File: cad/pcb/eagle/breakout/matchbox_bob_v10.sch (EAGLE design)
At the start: 9 parts, among them J1 DF12-32-DS, J2 DF12-32-DS

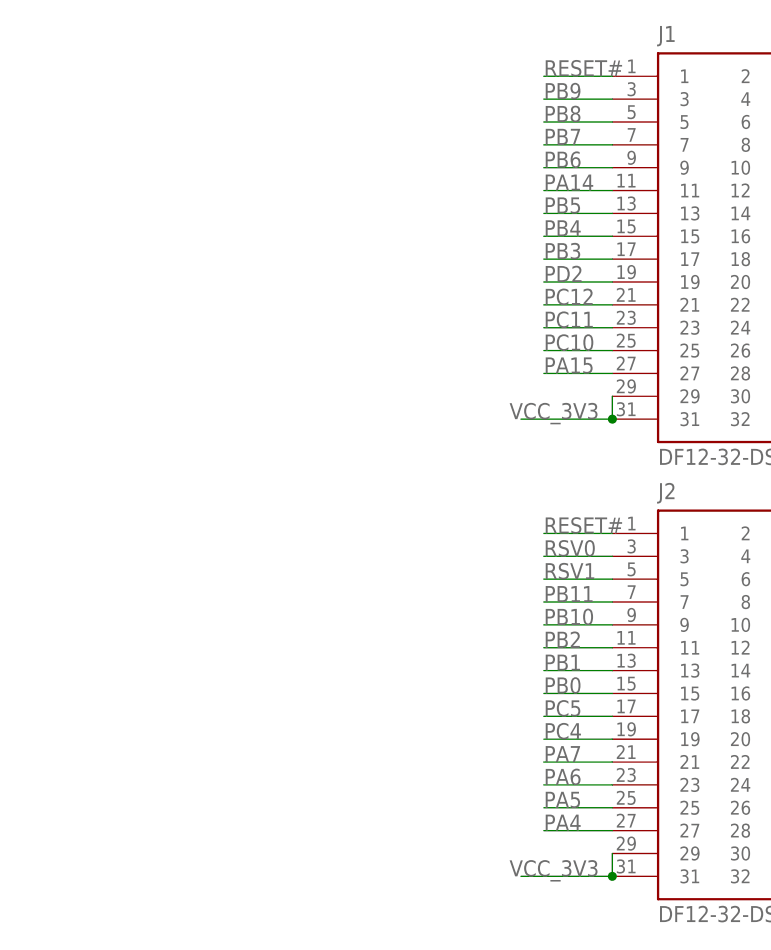
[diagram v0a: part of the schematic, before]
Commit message: Tweaks to BOB v1.0
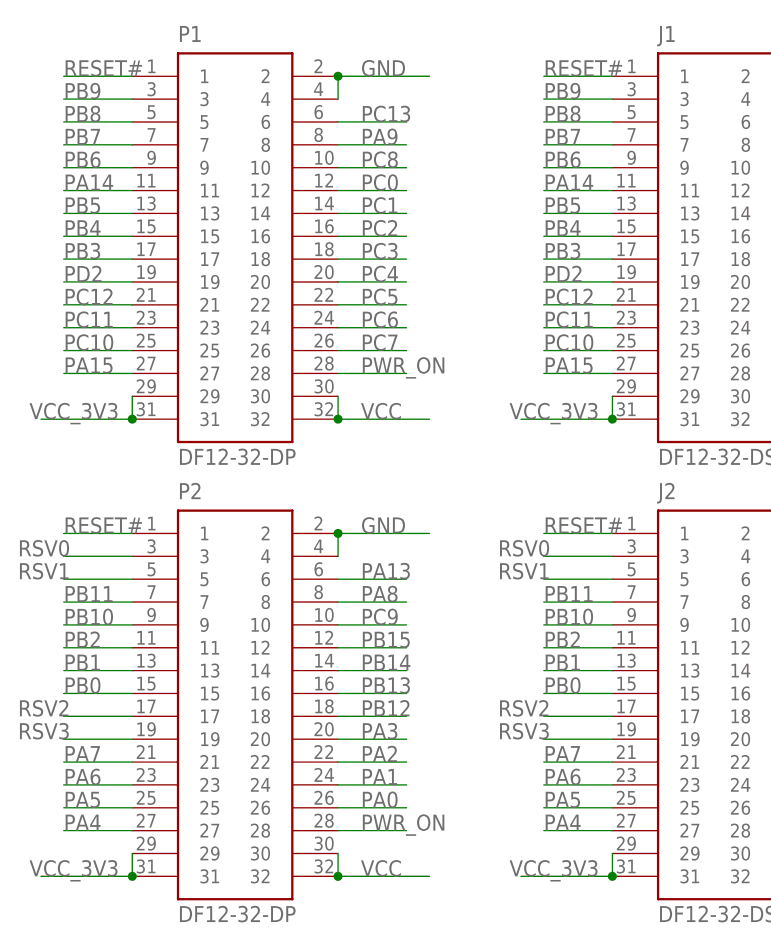
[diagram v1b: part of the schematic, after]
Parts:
- added P1, P2: DF12-32-DP, micro1292:AS-ITM-00015
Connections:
- new net RSV2: J2.17, P2.17
- new net RSV3: J2.19, P2.19
- net GND: now also P1.2, P1.4, P2.2, P2.4
- net PA0: now also P2.26
- net PA1: now also P2.24
- net PA13: now also P2.6
- net PA14: now also P1.11
- net PA15: now also P1.27
- net PA2: now also P2.22
- net PA3: now also P2.20
- net PA4: now also P2.27
- net PA5: now also P2.25
- net PA6: now also P2.23
- net PA7: now also P2.21
- net PA8: now also P2.8
- net PA9: now also P1.8
- net PB0: now also P2.15
- net PB1: now also P2.13
- net PB10: now also P2.9
- net PB11: now also P2.7
- net PB12: now also P2.18
- net PB13: now also P2.16
- net PB14: now also P2.14
- net PB15: now also P2.12
- net PB2: now also P2.11
- net PB3: now also P1.17
- net PB4: now also P1.15
- net PB5: now also P1.13
- net PB6: now also P1.9
- net PB7: now also P1.7
- net PB8: now also P1.5
- net PB9: now also P1.3
- net PC0: now also P1.12
- net PC1: now also P1.14
- net PC10: now also P1.25
- net PC11: now also P1.23
- net PC12: now also P1.21
- net PC13: now also P1.6
- net PC2: now also P1.16
- net PC3: now also P1.18
- net PC4: now also P1.20; no longer J2.19
- net PC5: now also P1.22; no longer J2.17
- net PC6: now also P1.24
- net PC7: now also P1.26
- net PC8: now also P1.10
- net PC9: now also P2.10
- net PD2: now also P1.19
- net PWR_ON: now also P1.28, P2.28
- net RESET#: now also P1.1, P2.1
- net RSV0: now also P2.3
- net RSV1: now also P2.5
- net VCC: now also P1.30, P1.32, P2.30, P2.32
- net VCC_3V3: now also P1.29, P1.31, P2.29, P2.31

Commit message: Add passthrough to v1.0 BOB
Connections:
- net PC4: now also J2.19
- net PC5: now also J2.17
- net RSV2: no longer J2.17
- net RSV3: no longer J2.19
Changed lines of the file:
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@@
 <net name="PC4" class="0">
+<segment>
+<wire x1="20.32" y1="81.28" x2="27.94" y2="81.28" width="0.1524" layer="91"/>
+<label x="20.32" y="81.28" size="1.778" layer="95"/>
+<pinref part="J2" gate="G$1" pin="19"/>
+</segment>
 <segment>
 <wire x1="50.8" y1="132.08" x2="58.42" y2="132.08" width="0.1524" layer="91"/>
@@
 <net name="PC5" class="0">
 <segment>
+<wire x1="20.32" y1="83.82" x2="27.94" y2="83.82" width="0.1524" layer="91"/>
+<label x="20.32" y="83.82" size="1.778" layer="95"/>
+<pinref part="J2" gate="G$1" pin="17"/>
+</segment>
+<segment>
 <wire x1="50.8" y1="129.54" x2="58.42" y2="129.54" width="0.1524" layer="91"/>
 <label x="53.34" y="129.54" size="1.778" layer="95"/>
@@
 <segment>
 <wire x1="20.32" y1="101.6" x2="27.94" y2="101.6" width="0.1524" layer="91"/>
-<label x="15.24" y="101.6" size="1.778" layer="95"/>
+<label x="20.32" y="101.6" size="1.778" layer="95"/>
 <pinref part="J2" gate="G$1" pin="3"/>
 </segment>
@@
 <segment>
 <wire x1="20.32" y1="99.06" x2="27.94" y2="99.06" width="0.1524" layer="91"/>
-<label x="15.24" y="99.06" size="1.778" layer="95"/>
+<label x="20.32" y="99.06" size="1.778" layer="95"/>
 <pinref part="J2" gate="G$1" pin="5"/>
 </segment>
@@
 <pinref part="P2" gate="G$1" pin="17"/>
 </segment>
-<segment>
-<wire x1="20.32" y1="83.82" x2="27.94" y2="83.82" width="0.1524" layer="91"/>
-<label x="15.24" y="83.82" size="1.778" layer="95"/>
-<pinref part="J2" gate="G$1" pin="17"/>
-</segment>
 </net>
 <net name="RSV3" class="0">
@@
 <pinref part="P2" gate="G$1" pin="19"/>
 </segment>
-<segment>
-<wire x1="20.32" y1="81.28" x2="27.94" y2="81.28" width="0.1524" layer="91"/>
-<label x="15.24" y="81.28" size="1.778" layer="95"/>
-<pinref part="J2" gate="G$1" pin="19"/>
-</segment>
-</net>
+</net>
